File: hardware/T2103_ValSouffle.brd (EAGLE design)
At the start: 81.3 x 67 mm, 38 parts, among them IC1 LM317MB, Q1 BSS101, T1 2N2222, U1 ATMEGA328P-PU, U2 SN74HC595N, X1 49S/18PF

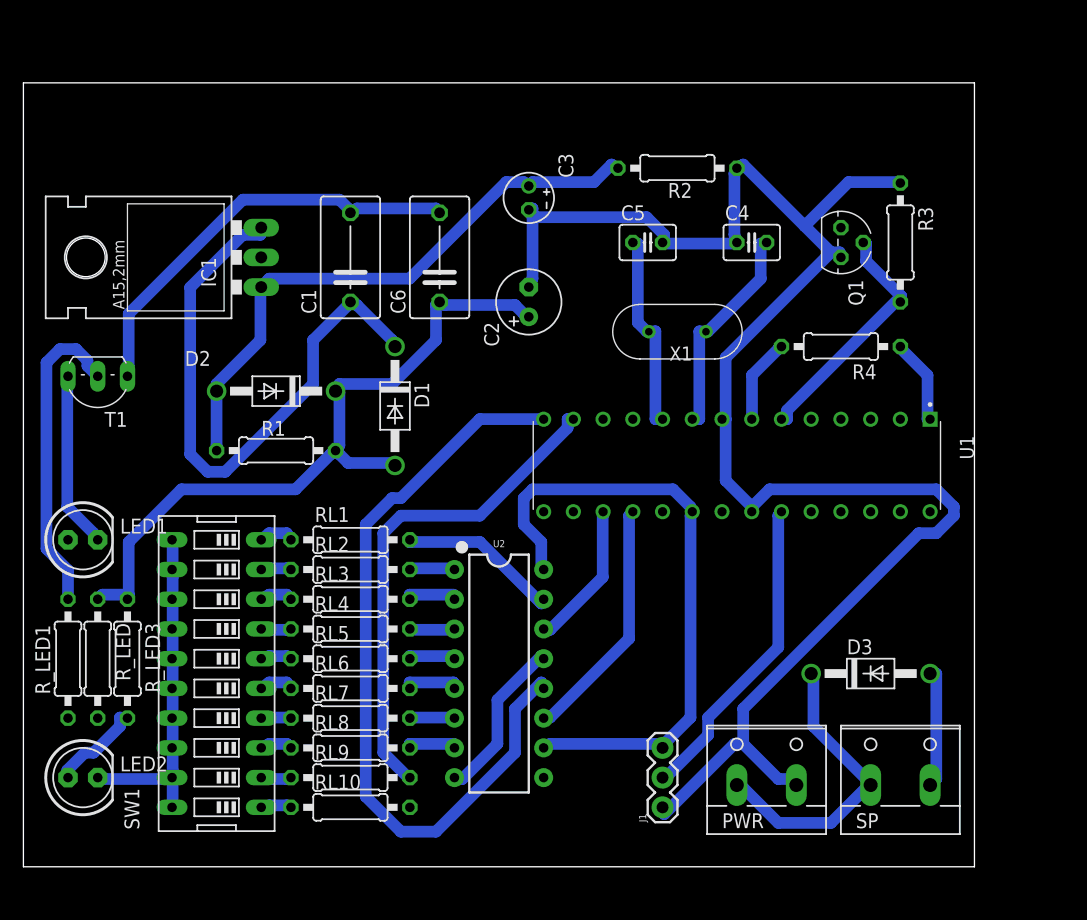
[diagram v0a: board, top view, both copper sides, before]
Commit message: finalize routing
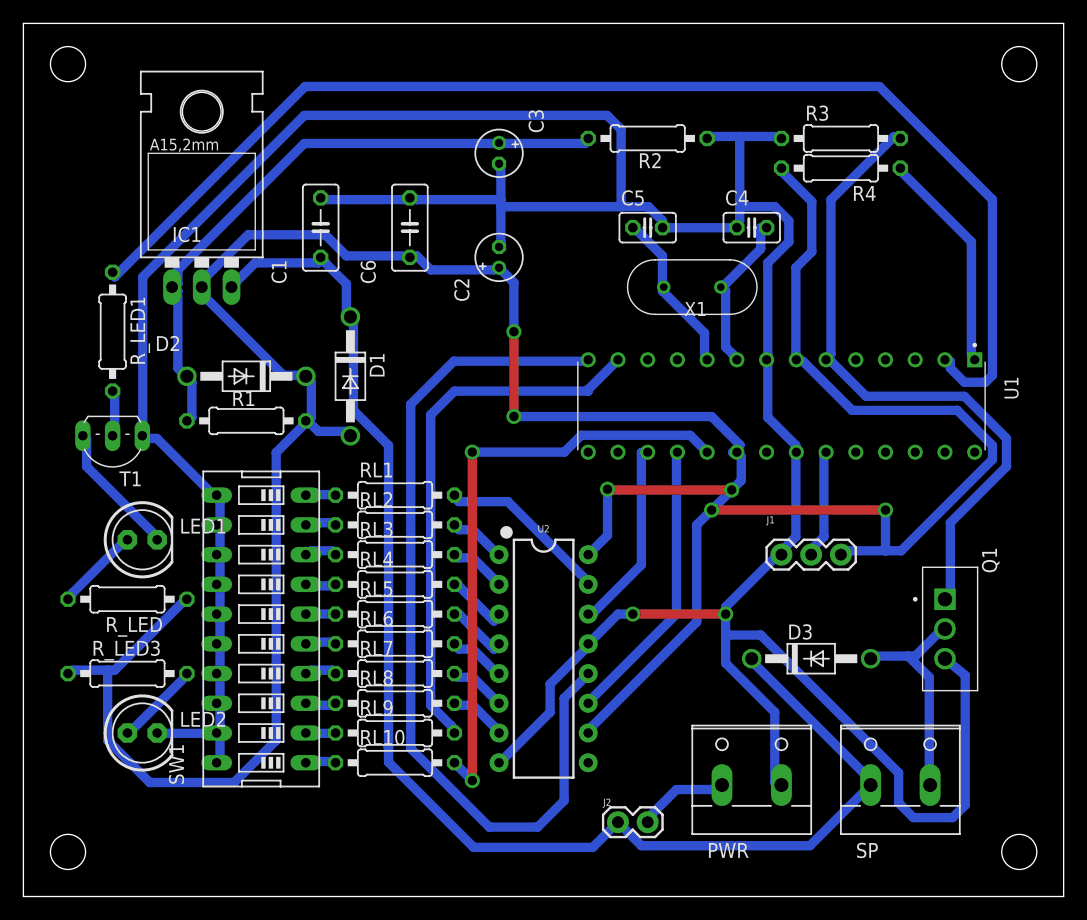
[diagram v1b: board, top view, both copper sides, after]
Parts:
- added J2: (no value), SparkFun-Connectors:1X02
- C1, C6: value 0.1uF -> 100n; device rcl:C075-052X106 -> rcl:C050-030X075
- C2: device resistor:E2,5-6 -> resistor:E1,8-4
- C3: device resistor:E2-4 -> resistor:E1,8-4
- C4, C5: value (none) -> 22p; device resistor:C025-030X050 -> resistor:C025-025X050
- Q1: value BSS101 -> IRFB4310ZPBF; device transistor-fet_220:TO92 -> Transistor:TO-220
- X1: value 49S/18PF -> 16Mhz
- moved Q1 31.8 mm to (78.7, 22.9)
- moved R_LED1 28.2 mm to (7.62, 45.7), turned to 270 degrees
- moved J1 23.9 mm to (64.8, 26.7), turned to 0 degrees
- moved R4 15.2 mm to (69.8, 59.7)
- moved R3 10.2 mm to (69.8, 62.2), turned to 0 degrees
- moved LED2 6.35 mm to (10.2, 11.4)
- moved U1 6.35 mm to (64.8, 39.4)
- moved R_LED 5.68 mm to (8.89, 22.9), turned to 180 degrees
- moved RL2 5.39 mm to (31.8, 29.2)
- moved RL3 5.39 mm to (31.8, 26.7)
- moved RL7 5.39 mm to (31.8, 16.5)
- moved RL10 5.39 mm to (31.8, 8.89)
- moved RL6 5.39 mm to (31.8, 19.1)
- moved RL8 5.39 mm to (31.8, 14.0)
- moved RL1 5.39 mm to (31.8, 31.8)
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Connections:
- new net VCCSHUT: J2.2, PWR.1
- net GND: now also Q1.S; no longer Q1.1
- net N$4: now also Q1.G; no longer Q1.2
- net SP2: now also Q1.D; no longer Q1.3
- net VCC12: now also J2.1; no longer PWR.1
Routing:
- net VCC: track 122.8 -> 269.8 mm, vias 0 -> 6
- net PFFT: track 0.00 -> 106.6 mm
- net GND: track 225.7 -> 292.2 mm, vias 0 -> 2
- net D10: track 0.00 -> 51.5 mm, vias 0 -> 2
- net VCC12: track 76.5 -> 117.6 mm
- net N$4: track 21.5 -> 56.1 mm
- net N$21: track 27.1 -> 3.89 mm
- net N$17: track 27.2 -> 9.43 mm
- net N$5: track 7.36 -> 18.9 mm
- net SP2: track 10.3 -> 19.2 mm
- net ST_CP: track 66.4 -> 74.7 mm
- net VCCSHUT: track 0.00 -> 7.87 mm
- net N$18: track 0.00 -> 7.20 mm
- net N$2: track 18.7 -> 13.8 mm
- net DS: track 12.5 -> 16.4 mm
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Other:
- board size 81.3 x 67 mm -> 88.9 x 74.6 mm

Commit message: Add manual switch
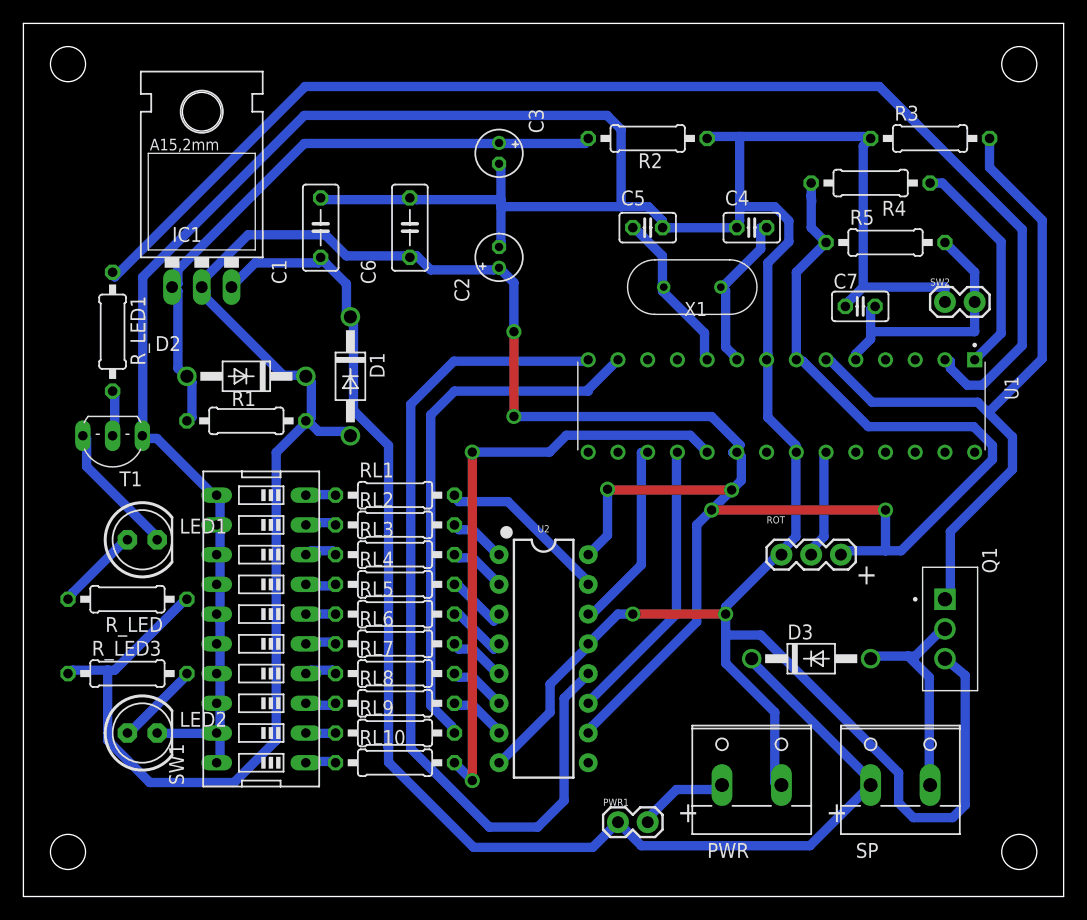
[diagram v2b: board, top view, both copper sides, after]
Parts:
- added C7: 10n, resistor:C025-025X050
- added R5: 10K, resistor:0207/10
- added SW2: (no value), SparkFun-Connectors:1X02
- moved R3 7.62 mm to (77.5, 62.2)
- moved R4 2.84 mm to (72.4, 58.4)
- renumbered J1 to ROT, J2 to PWR1
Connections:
- new net N$22: C7.2, R5.2, SW2.2, U1.5
- net GND: now also C7.1, SW2.1
- net VCC: now also R5.1
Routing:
- net GND: track 292.2 -> 323.3 mm
- net N$22: track 0.00 -> 22.9 mm
- net N$4: track 56.1 -> 62.1 mm
- net PFFT: track 106.6 -> 108.9 mm
- net VCC: track 269.8 -> 269.0 mm
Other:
- board text added: "+"

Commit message: Hardware update
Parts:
- R1: value 240Ω -> 220
- R2: value 720Ω -> 649
- R4: value 5k -> 10K
- RL1, RL10, RL2, RL3, RL4, RL5, RL6, RL7, RL8: value (none) -> 220
- RL9: value (none) -> 200
- R_LED, R_LED3: value 68 -> 220
- R_LED1: value 68 -> 10K

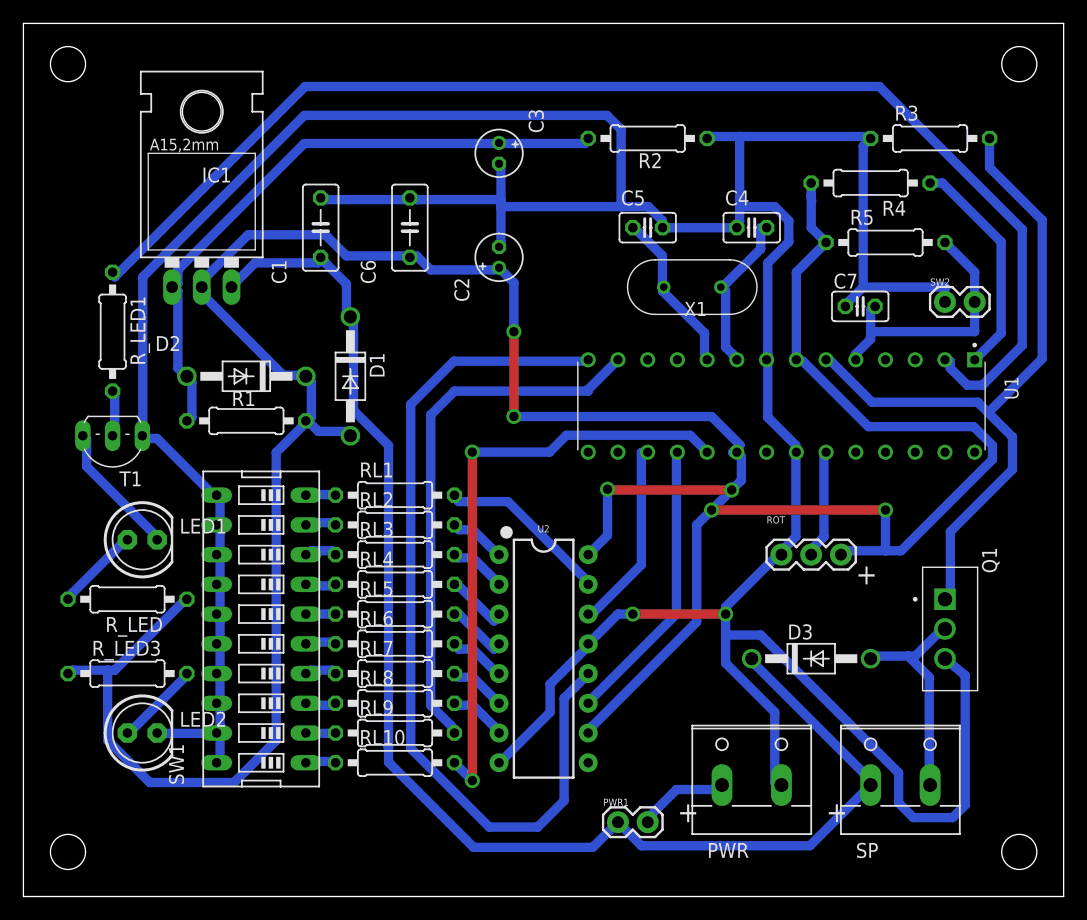
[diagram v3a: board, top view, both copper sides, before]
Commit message: update graph
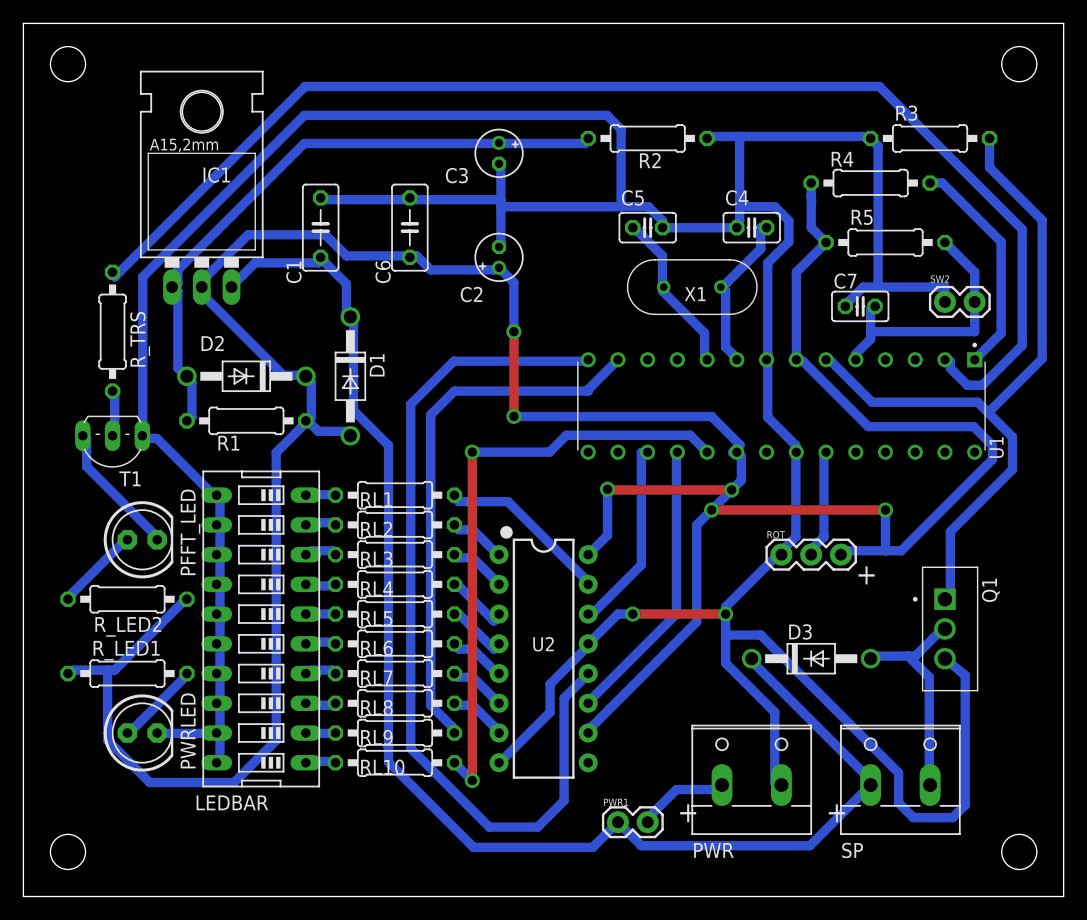
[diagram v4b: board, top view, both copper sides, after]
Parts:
- removed R_LED3: 220, resistor:0207/10
- added R_TRS: 10K, resistor:0207/10
- R1, R2: device resistor:0207/10 -> rcl:0207/10
- R_LED1: value 10K -> 220
- moved R_LED1 29.2 mm to (8.89, 16.5), turned to 0 degrees
- renumbered LED1 to PFFT_LED, LED2 to PWRLED, R_LED to R_LED2, SW1 to LEDBAR
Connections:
- net N$20: now also R_LED1.2; no longer R_LED3.2
- net N$21: now also R_TRS.2; no longer R_LED1.2
- net PFFT: now also R_TRS.1; no longer R_LED1.1
- net VCC: now also R_LED1.1; no longer R_LED3.1
